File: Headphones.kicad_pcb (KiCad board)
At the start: 2 copper layers, 58.2 x 107.4 mm, 52 parts, among them IC1 IP2326, IC2 MAX9744ETH+T, IC3 UDA1334ATS_N2,118, J2 USB4105-GF-A, U1 MOUDLE-SEEEDUINO-XIAO-ESP32C3

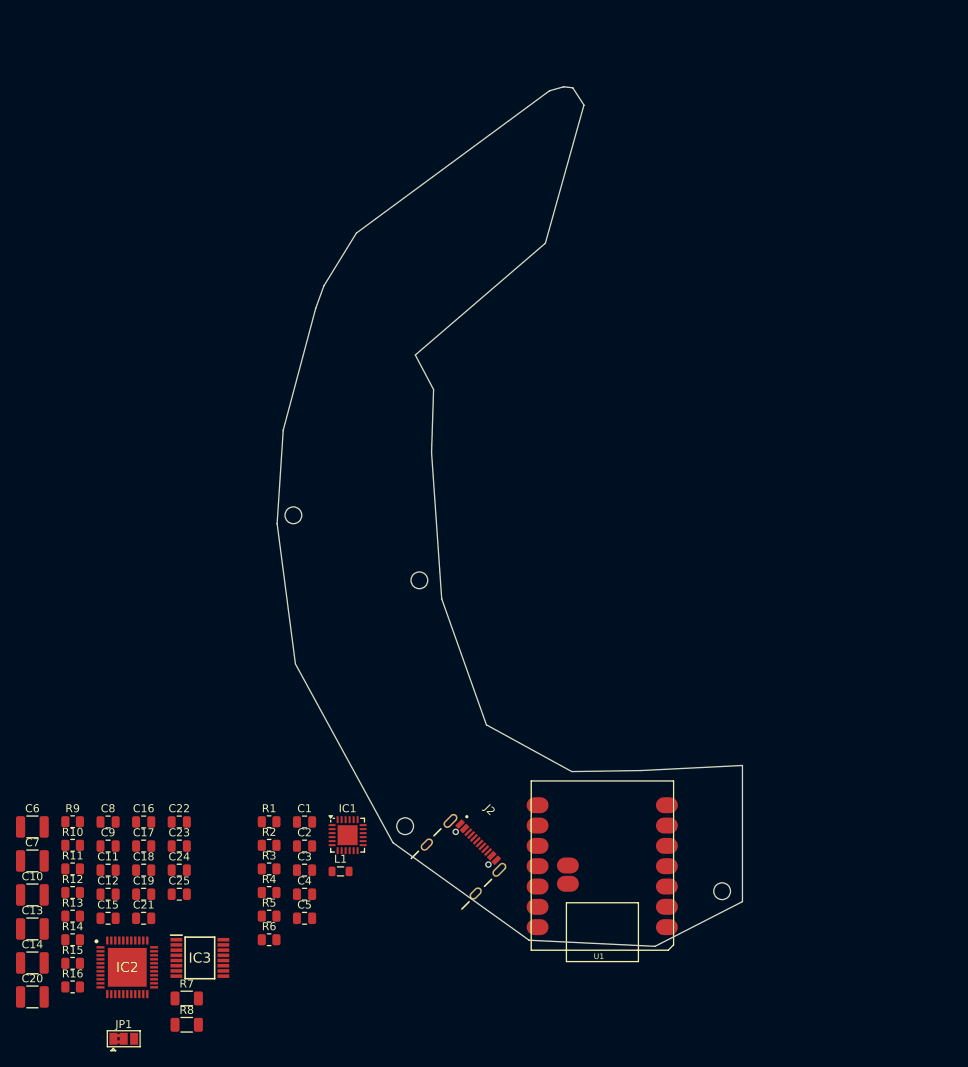
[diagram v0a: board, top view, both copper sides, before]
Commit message: Minor updates
Might need more room for the esp32. With the new USB connector the board space is very tight
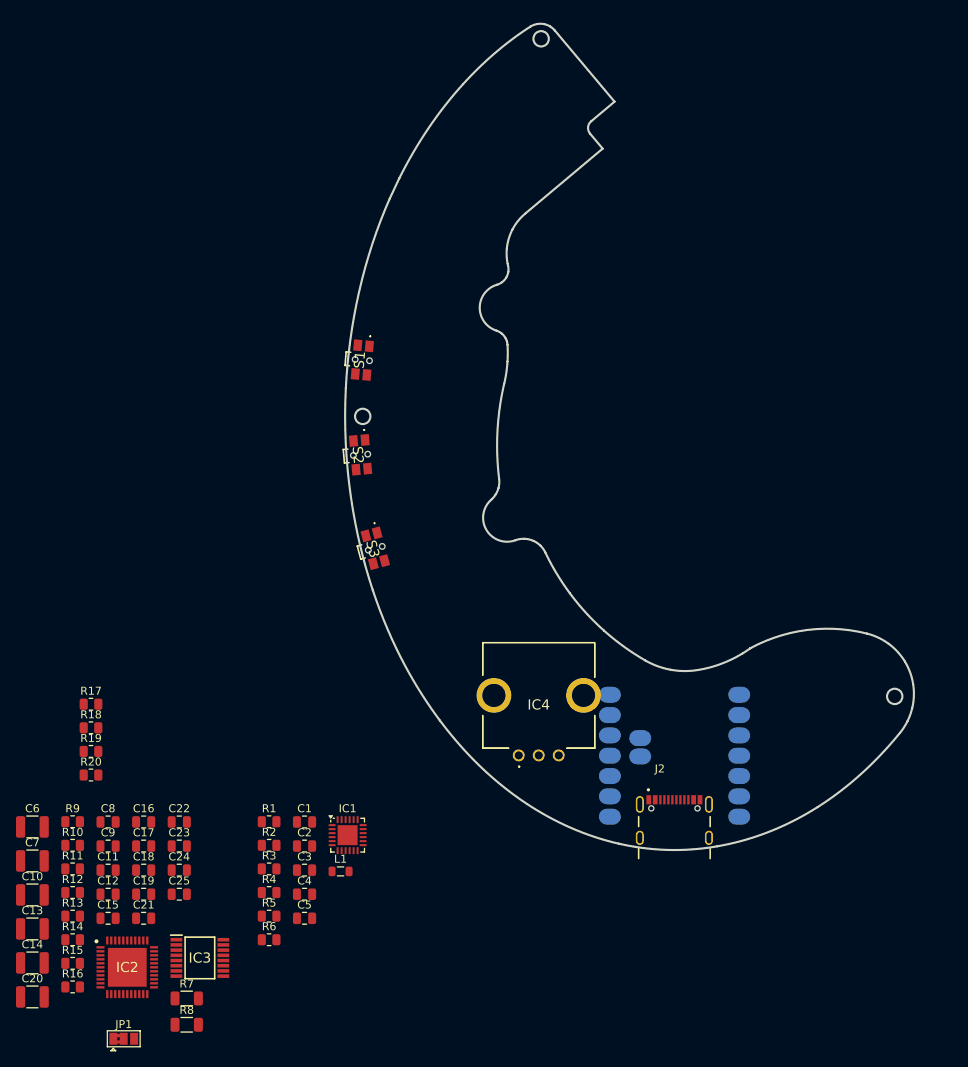
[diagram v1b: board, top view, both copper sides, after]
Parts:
- removed ? (x4): , clipboard:481d829e-8df2-4d8c-86dd-5558698f89fa
- added IC4: EC12E2430803, SamacSys_Parts:EC12E2430803, F.Cu at (116.8, 138.9)
- added R17: 4.7M, Resistor_SMD:R_0805_2012Metric, F.Cu at (63.3, 132.6)
- added R18: 2.2M, Resistor_SMD:R_0805_2012Metric, F.Cu at (63.3, 135.5)
- added R19: 1M, Resistor_SMD:R_0805_2012Metric, F.Cu at (63.3, 138.5)
- added R20: 1M, Resistor_SMD:R_0805_2012Metric, F.Cu at (63.3, 141.4)
- added S1: EVQ-P7C01P, SamacSys_Parts:EVQP7C01P, F.Cu at (96.9, 89.5)
- added S2: EVQ-P7C01P, SamacSys_Parts:EVQP7C01P, F.Cu at (96.7, 101.4)
- added S3: EVQ-P7C01P, SamacSys_Parts:EVQP7C01P, F.Cu at (98.6, 113.1)
- U1: moved to B.Cu
- moved J2 28.2 mm to (136.3, 149.3), turned to 0 degrees
- moved U1 11.5 mm to (145.2, 149.5)
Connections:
- U1 pad 1: unconnected-(U1-PA02_A0_D0-Pad1) -> Buttons
- U1 pad 2: unconnected-(U1-PA4_A1_D1-Pad2) -> Net-(U1-PA4_A1_D1)
- U1 pad 3: unconnected-(U1-PA10_A2_D2-Pad3) -> Net-(U1-PA10_A2_D2)
- U1 pad 4: unconnected-(U1-PA11_A3_D3-Pad4) -> Net-(U1-PA11_A3_D3)
- U1 pad 5: unconnected-(U1-PA8_A4_D4_SDA-Pad5) -> Net-(U1-PA8_A4_D4_SDA)
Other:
- board size 58.2 x 107.4 mm -> 71.1 x 103.3 mm

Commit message: Rev1 Update
Layout and traces done. 3d model done. Need to review layout placement and schematic. Change amp and dsp for lower cost??
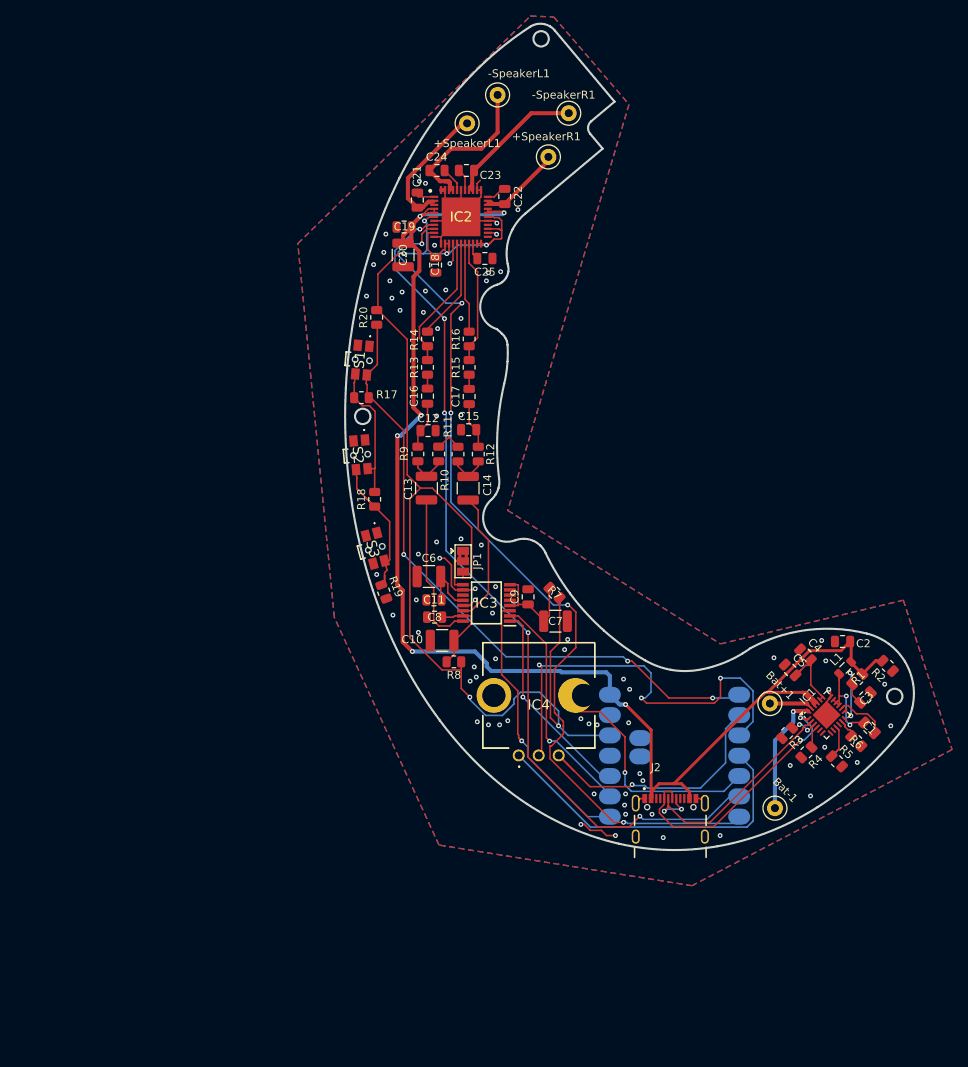
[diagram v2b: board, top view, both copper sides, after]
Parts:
- added +SpeakerL1: TestPoint, TestPoint:TestPoint_Loop_D1.80mm_Drill1.0mm_Beaded, F.Cu at (110.4, 59.9)
- added +SpeakerR1: TestPoint, TestPoint:TestPoint_Loop_D1.80mm_Drill1.0mm_Beaded, F.Cu at (120.5, 64.1)
- added -SpeakerL1: TestPoint, TestPoint:TestPoint_Loop_D1.80mm_Drill1.0mm_Beaded, F.Cu at (114.2, 56.4)
- added -SpeakerR1: TestPoint, TestPoint:TestPoint_Loop_D1.80mm_Drill1.0mm_Beaded, F.Cu at (123.1, 58.7)
- added Bat+1: TestPoint, TestPoint:TestPoint_Loop_D1.80mm_Drill1.0mm_Beaded, F.Cu at (148.2, 132.5)
- added Bat-1: TestPoint, TestPoint:TestPoint_Loop_D1.80mm_Drill1.0mm_Beaded, F.Cu at (148.8, 145.5)
- R7, R8: footprint Resistor_SMD:R_1206_3216Metric -> Resistor_SMD:R_0805_2012Metric
- moved C20 103.7 mm to (102.4, 76.4), turned to 90 degrees
- moved IC2 102.7 mm to (109.6, 71.6)
- moved C21 96.1 mm to (104.1, 69.5), turned to -90 degrees
- moved R16 95.0 mm to (110.6, 86.9), turned to 90 degrees
- moved C24 93.2 mm to (106.6, 65.8), turned to 180 degrees
- moved C23 91.8 mm to (110.3, 65.8)
- moved C19 89.5 mm to (102.5, 72.9)
- moved R15 89.5 mm to (110.6, 90.4), turned to 90 degrees
- moved C25 88.2 mm to (112.6, 76.8), turned to 180 degrees
- moved C22 88.1 mm to (115.1, 69.1), turned to -90 degrees
- moved R14 87.2 mm to (105.4, 86.9), turned to 90 degrees
- moved C18 84.0 mm to (106.4, 77.7), turned to -90 degrees
- moved R13 81.7 mm to (105.4, 90.4), turned to 90 degrees
- moved C14 80.5 mm to (110.5, 105.6), turned to 90 degrees
- moved R2 80.5 mm to (162.9, 127.8), turned to 135 degrees
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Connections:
- IC1 pad 21: VOUT -> VBUS
- IC1 pad 22: VOUT -> VBUS
- IC1 pad 23: VBATM -> VBATP
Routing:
- net VBUS: track 0.00 -> 176.8 mm, vias 0 -> 6
- net +3.3V: track 0.00 -> 159.1 mm, vias 0 -> 6
- net SCLK/PWM: track 0.00 -> 112.4 mm, vias 0 -> 5
- net SDA/VOL: track 0.00 -> 108.4 mm, vias 0 -> 5
- net Buttons: track 0.00 -> 81.2 mm, vias 0 -> 3
- net GND: track 0.00 -> 55.7 mm, vias 0 -> 75
- net Net-(U1-PA10_A2_D2): track 0.00 -> 55.2 mm, vias 0 -> 3
- net Net-(U1-PA11_A3_D3): track 0.00 -> 42.9 mm
- net Net-(U1-PA4_A1_D1): track 0.00 -> 35.0 mm, vias 0 -> 1
- net Net-(IC3-DATAI): track 0.00 -> 34.0 mm, vias 0 -> 1
- net Net-(IC1-DM): track 0.00 -> 33.2 mm, vias 0 -> 2
- net Net-(IC1-DP): track 0.00 -> 30.3 mm, vias 0 -> 2
- net Net-(U1-PA8_A4_D4_SDA): track 0.00 -> 29.0 mm, vias 0 -> 1
- net Net-(IC3-WS): track 0.00 -> 28.9 mm, vias 0 -> 1
- net Net-(IC3-BCK): track 0.00 -> 25.7 mm, vias 0 -> 1
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- added copper zone on B.Cu, net GND
- added copper zone on F.Cu, net GND
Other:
- outline, holes or cut-outs redrawn
